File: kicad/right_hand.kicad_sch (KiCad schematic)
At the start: 29 parts, among them SW34 Gateron_ks_27, SW35 Gateron_ks_27, SW36 Gateron_ks_27, SW37 Gateron_ks_27, SW38 Gateron_ks_27, SW39 Gateron_ks_27, SW40 Gateron_ks_27, SW41 Gateron_ks_27, SW42 Gateron_ks_27, SW43 Gateron_ks_27, SW44 Gateron_ks_27, SW45 Gateron_ks_27, SW46 Gateron_ks_27, SW47 Gateron_ks_27, SW48 Gateron_ks_27, SW49 Gateron_ks_27, SW50 Gateron_ks_27, SW51 Gateron_ks_27, SW52 Gateron_ks_27, SW53 Gateron_ks_27, SW54 Gateron_ks_27, SW55 Gateron_ks_27, SW56 Gateron_ks_27, SW57 Gateron_ks_27, SW58 Gateron_ks_27, SW59 Gateron_ks_27, SW60 Gateron_ks_27, SW61 Gateron_ks_27, U3 74HC595

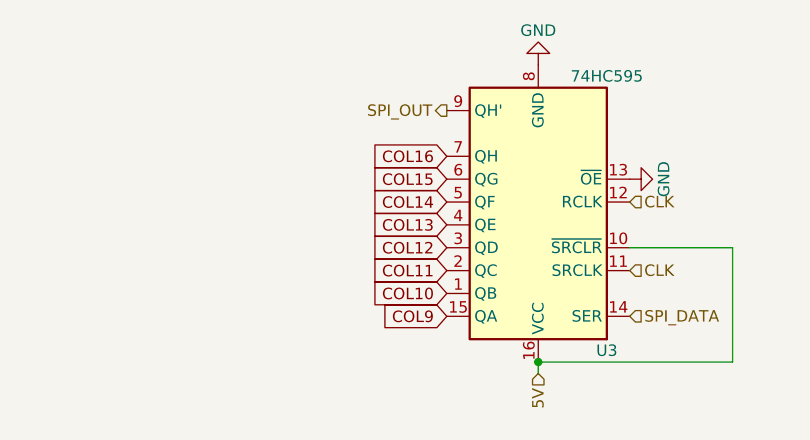
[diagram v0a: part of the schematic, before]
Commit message: Update switch diode
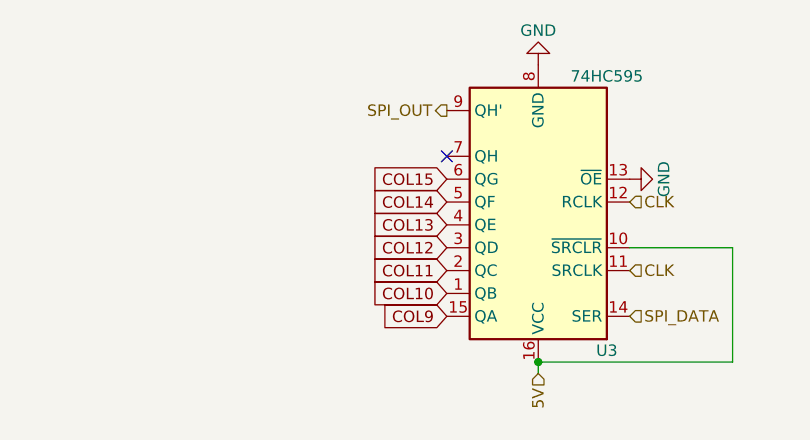
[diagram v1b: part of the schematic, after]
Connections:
- net COL16: no longer names the net of U3.7 (QH)
- no-connect marks 0 -> 1

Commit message: Update PCB
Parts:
- added D31, D32, D33, D34, D35, D36, D37, D38, D39, D40, D41, D42, D43, D44, D45, D46, D47, D48, D49, D50, D51, D52, D53, D54, D55, D56, D57, D58: 1N4148W, Diode_SMD:D_SOD-123, symbol Diode:1N4148W-JLC
- SW34, SW35, SW36, SW37, SW38, SW39, SW40, SW41, SW42, SW43, SW44, SW45, SW46, SW47, SW48, SW49, SW50, SW51, SW52, SW53, SW54, SW55, SW56, SW57, SW58, SW59, SW60, SW61: now not fitted
- U3: LCSC (none) -> C72115
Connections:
- net ROW1: now also D31.1 (K), D32.1 (K), D33.1 (K), D34.1 (K), D35.1 (K), D36.1 (K), D37.1 (K); no longer SW34.3 (K), SW38.3 (K), SW42.3 (K), SW46.3 (K), SW50.3 (K), SW54.3 (K), SW58.3 (K)
- net ROW2: now also D38.1 (K), D39.1 (K), D40.1 (K), D41.1 (K), D42.1 (K), D43.1 (K), D44.1 (K); no longer SW35.3 (K), SW39.3 (K), SW43.3 (K), SW47.3 (K), SW51.3 (K), SW55.3 (K), SW59.3 (K)
- net ROW3: now also D45.1 (K), D46.1 (K), D47.1 (K), D48.1 (K), D49.1 (K), D50.1 (K), D51.1 (K); no longer SW36.3 (K), SW40.3 (K), SW44.3 (K), SW48.3 (K), SW52.3 (K), SW56.3 (K), SW60.3 (K)
- net ROW4: now also D52.1 (K), D53.1 (K), D54.1 (K), D55.1 (K), D56.1 (K), D57.1 (K), D58.1 (K); no longer SW37.3 (K), SW41.3 (K), SW45.3 (K), SW49.3 (K), SW53.3 (K), SW57.3 (K), SW61.3 (K)
- net at SW51.1: now also D42.2 (A); no longer SW51.4 (A)
- net at SW38.1: now also D32.2 (A); no longer SW38.4 (A)
- net at SW52.1: now also D49.2 (A); no longer SW52.4 (A)
- net at SW46.1: now also D34.2 (A); no longer SW46.4 (A)
- net at SW39.1: now also D39.2 (A); no longer SW39.4 (A)
- net at SW35.1: now also D38.2 (A); no longer SW35.4 (A)
- net at SW43.1: now also D40.2 (A); no longer SW43.4 (A)
- net at SW48.1: now also D48.2 (A); no longer SW48.4 (A)
- net at SW41.1: now also D53.2 (A); no longer SW41.4 (A)
- net at SW56.1: now also D50.2 (A); no longer SW56.4 (A)
- net at SW50.1: now also D35.2 (A); no longer SW50.4 (A)
- net at SW40.1: now also D46.2 (A); no longer SW40.4 (A)
- net at SW34.1: now also D31.2 (A); no longer SW34.4 (A)
- net at SW57.1: now also D57.2 (A); no longer SW57.4 (A)
- net at SW58.1: now also D37.2 (A); no longer SW58.4 (A)
- net at SW37.1: now also D52.2 (A); no longer SW37.4 (A)
- net at SW47.1: now also D41.2 (A); no longer SW47.4 (A)
- net at SW36.1: now also D45.2 (A); no longer SW36.4 (A)
- net at SW49.1: now also D55.2 (A); no longer SW49.4 (A)
- net at SW60.1: now also D51.2 (A); no longer SW60.4 (A)
- net at SW44.1: now also D47.2 (A); no longer SW44.4 (A)
- net at SW61.1: now also D58.2 (A); no longer SW61.4 (A)
- net at SW54.1: now also D36.2 (A); no longer SW54.4 (A)
- net at SW53.1: now also D56.2 (A); no longer SW53.4 (A)
- net at SW42.1: now also D33.2 (A); no longer SW42.4 (A)
- net at SW59.1: now also D44.2 (A); no longer SW59.4 (A)
- net at SW45.1: now also D54.2 (A); no longer SW45.4 (A)
- net at SW55.1: now also D43.2 (A); no longer SW55.4 (A)

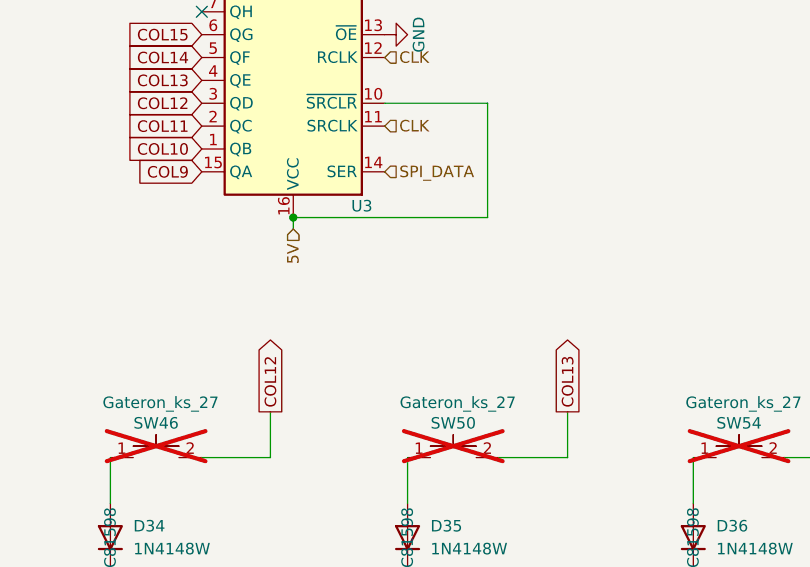
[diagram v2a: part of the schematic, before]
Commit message: SIPO is SMT
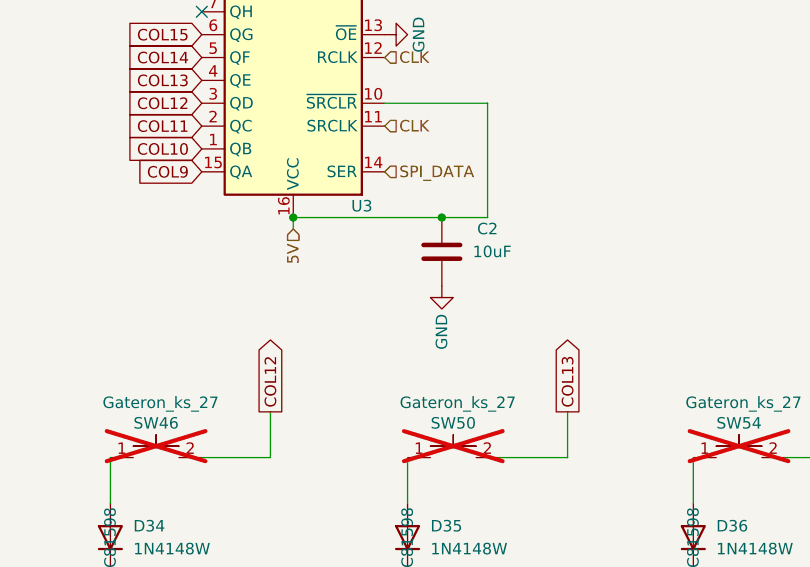
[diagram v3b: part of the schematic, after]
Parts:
- added C2: 10uF, Capacitor_SMD:C_0603_1608Metric, symbol Device:C
- U3: footprint Package_DIP:DIP-16_W7.62mm_Socket -> Package_SO:SO-16_3.9x9.9mm_P1.27mm; LCSC C72115 -> C5947
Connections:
- net 5V: now also C2.1
- net GND: now also C2.2
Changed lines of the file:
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@@
 	)
 	(junction
+		(at 220.98 83.82)
+		(diameter 0)
+		(color 0 0 0 0)
+	)
+	(junction
 		(at 119.38 157.48)
 		(diameter 0)
@@
 	(wire
 		(pts
+			(xy 220.98 83.82) (xy 226.06 83.82)
+		)
+		(stroke
+			(width 0)
+			(type default)
+		)
+	)
+	(wire
+		(pts
 			(xy 299.72 110.49) (xy 299.72 105.41)
 		)
@@
 	(wire
 		(pts
-			(xy 204.47 83.82) (xy 226.06 83.82)
+			(xy 204.47 83.82) (xy 220.98 83.82)
 		)
 		(stroke
@@
 			)
 		)
-		(property "Footprint" "Package_DIP:DIP-16_W7.62mm_Socket"
+		(property "Footprint" "Package_SO:SO-16_3.9x9.9mm_P1.27mm"
 			(at 204.47 68.58 0)
 			(effects
@@
 			)
 		)
-		(property "LCSC" "C72115"
+		(property "LCSC" "C5947"
 			(at 204.47 68.58 0)
 			(effects
@@
 	)
 	(symbol
+		(lib_id "Device:C")
+		(at 220.98 87.63 0)
+		(unit 1)
+		(exclude_from_sim no)
+		(in_bom yes)
+		(on_board yes)
+		(dnp no)
+		(property "Reference" "C2"
+			(at 226.06 85.09 0)
+			(effects
+				(font
+					(size 1.27 1.27)
+				)
+			)
+		)
+		(property "Value" "10uF"
+			(at 226.568 87.63 0)
+			(effects
+				(font
+					(size 1.27 1.27)
+				)
+			)
+		)
+		(property "Footprint" "Capacitor_SMD:C_0603_1608Metric"
+			(at 221.9452 91.44 0)
+			(effects
+				(font
+					(size 1.27 1.27)
+				)
+				(hide yes)
+			)
+		)
+		(property "Datasheet" "~"
+			(at 220.98 87.63 0)
+			(effects
+				(font
+					(size 1.27 1.27)
+				)
+				(hide yes)
+			)
+		)
+		(property "Description" ""
+			(at 220.98 87.63 0)
+			(effects
+				(font
+					(size 1.27 1.27)
+				)
+				(hide yes)
+			)
+		)
+		(property "LCSC" "C19702"
+			(at 220.98 87.63 90)
+			(effects
+				(font
+					(size 1.27 1.27)
+				)
+				(hide yes)
+			)
+		)
+		(pin "1"
+		)
+		(pin "2"
+		)
+		(instances
+			(project "keyboard"
+				(path "/b0ce3c94-e169-4400-82ce-8ef44a8a59a3/7618c816-4ebe-48b1-bd99-e5bb32d58cf0"
+					(reference "C2")
+					(unit 1)
+				)
+			)
+		)
+	)
+	(symbol
 		(lib_id "Diode:1N4148W-JLC")
 		(at 281.94 214.63 90)
@@
 					(unit 1)
 				)
+			)
+		)
+	)
+	(symbol
+		(lib_id "power:GND")
+		(at 220.98 91.44 0)
+		(unit 1)
+		(exclude_from_sim no)
+		(in_bom yes)
+		(on_board yes)
+		(dnp no)
+		(property "Reference" "#PWR04"
+			(at 220.98 97.79 0)
+			(effects
+				(font
+					(size 1.27 1.27)
+				)
+				(hide yes)
+			)
+		)
+		(property "Value" "GND"
+			(at 220.98 96.52 90)
+			(effects
+				(font
+					(size 1.27 1.27)
+				)
+			)
+		)
+		(property "Footprint" ""
+			(at 220.98 91.44 0)
+			(effects
+				(font
+					(size 1.27 1.27)
+				)
+				(hide yes)
+			)
+		)
+		(property "Datasheet" ""
+			(at 220.98 91.44 0)
+			(effects
+				(font
+					(size 1.27 1.27)
+				)
+				(hide yes)
+			)
+		)
+		(property "Description" "Power symbol creates a global label with name \"GND\" , ground"
+			(at 220.98 91.44 0)
+			(effects
+				(font
+					(size 1.27 1.27)
+				)
+				(hide yes)
+			)
+		)
+		(pin "1"
+		)
+		(instances
+			(project "keyboard"
+				(path "/b0ce3c94-e169-4400-82ce-8ef44a8a59a3/7618c816-4ebe-48b1-bd99-e5bb32d58cf0"
+					(reference "#PWR04")
+					(unit 1)
+				)
